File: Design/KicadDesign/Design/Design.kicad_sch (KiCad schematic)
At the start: 10 parts, among them J3 Jack 3.5 mm, Q1 IRLZ44N, Q2 IRLZ44N, U1 IR2110

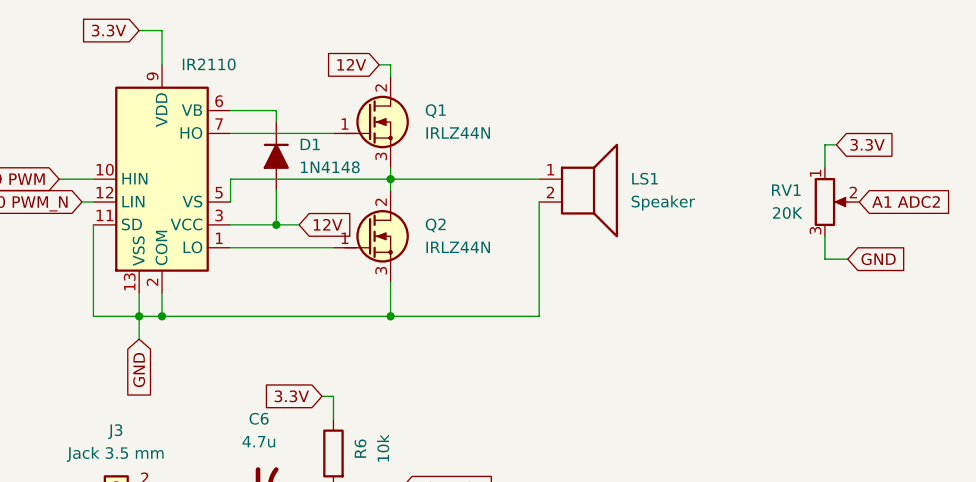
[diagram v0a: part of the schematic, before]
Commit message: Added Caps on VB TODO: Add STM32H523cet6 Footprint
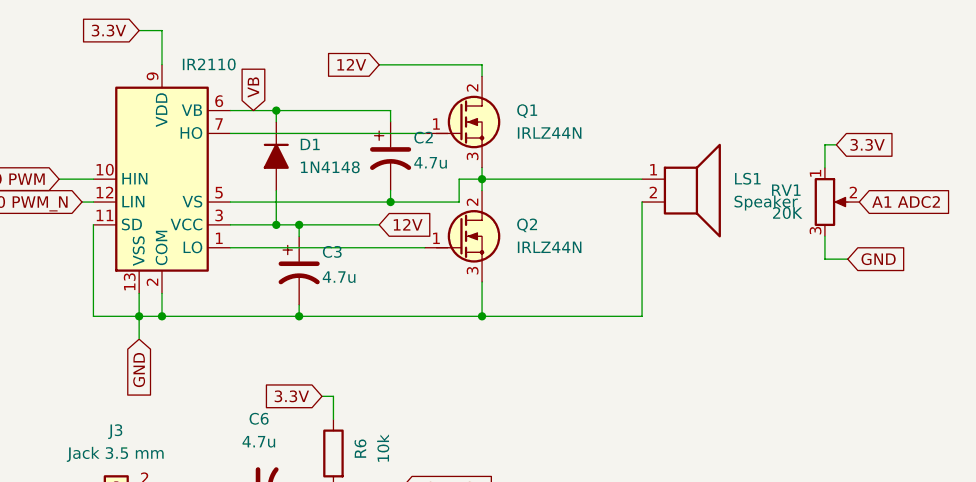
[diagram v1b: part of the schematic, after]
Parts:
- added C2, C3: 4.7u, Capacitor_THT:CP_Radial_D10.0mm_P3.50mm, symbol Device:C_Polarized_US
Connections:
- net 12V: now also C3.1
- net GND: now also C3.2
- net at LS1.1, Q1.3 (S), Q2.2 (D)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: now also C2.2
- net VB: now reaches D1.1 (K), U1.6 (VB)
- net VB: now also C2.1
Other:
- moved on the sheet: LS1, Q1, Q2

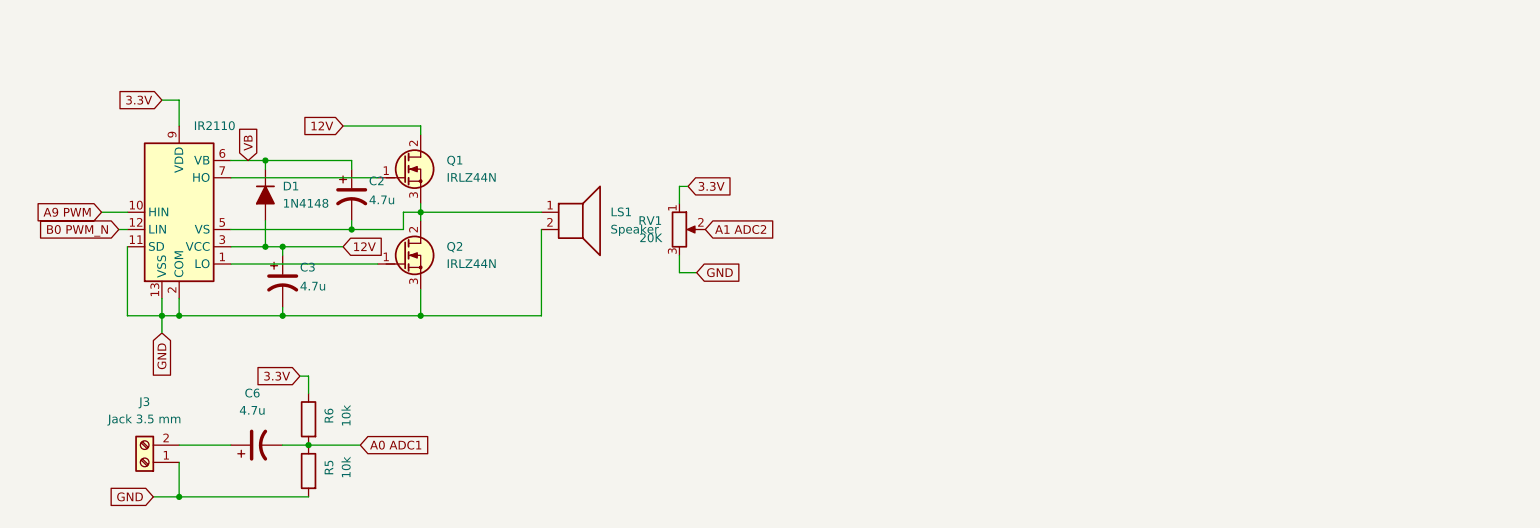
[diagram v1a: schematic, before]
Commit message: Added LC Filter
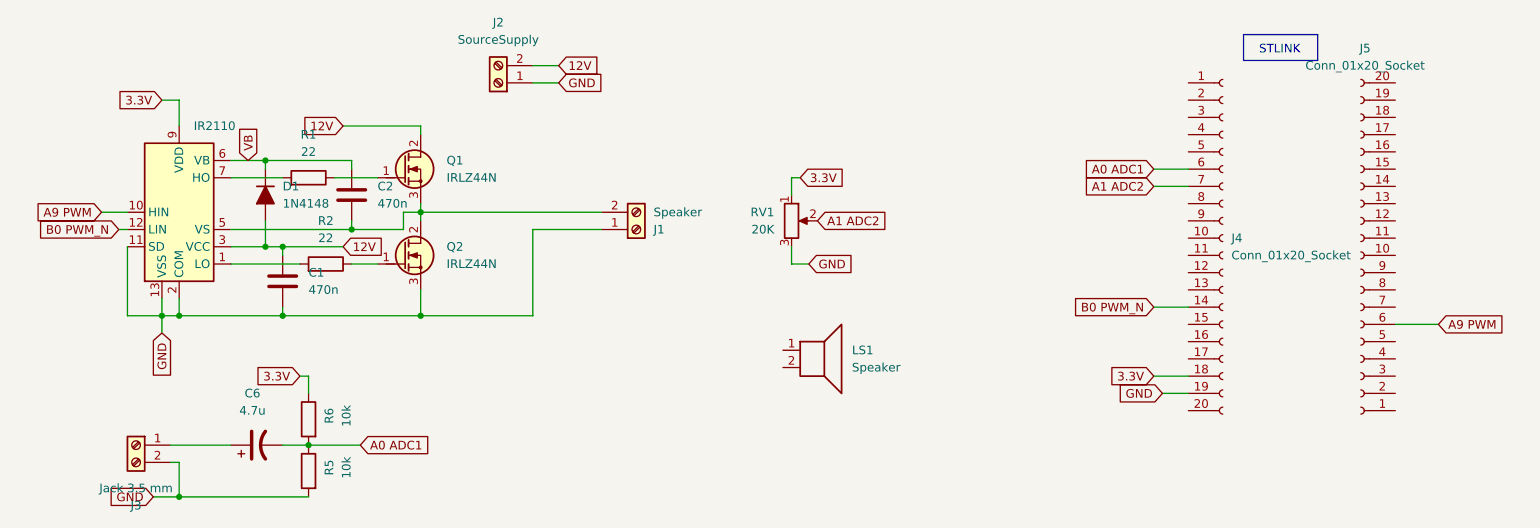
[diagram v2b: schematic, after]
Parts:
- removed C2, C3: 4.7u, Capacitor_THT:CP_Radial_D10.0mm_P3.50mm, symbol Device:C_Polarized_US
- added C1, C2: 470n, Capacitor_THT:C_Disc_D3.8mm_W2.6mm_P2.50mm, symbol PCM_Capacitor_AKL:C_0201
- added J1: Speaker, TerminalBlock:TerminalBlock_MaiXu_MX126-5.0-02P_1x02_P5.00mm, symbol Connector:Screw_Terminal_01x02
- added J2: SourceSupply, TerminalBlock:TerminalBlock_MaiXu_MX126-5.0-02P_1x02_P5.00mm, symbol Connector:Screw_Terminal_01x02
- added J4, J5: Conn_01x20_Socket, Connector_PinHeader_2.54mm:PinHeader_1x20_P2.54mm_Vertical, symbol Connector:Conn_01x20_Socket
- added R1, R2: 22, Resistor_THT:R_Axial_DIN0204_L3.6mm_D1.6mm_P7.62mm_Horizontal, symbol PCM_Resistor_AKL:R_0201
- C6: footprint Capacitor_THT:CP_Radial_D10.0mm_P3.50mm -> Capacitor_THT:CP_Radial_D5.0mm_P2.50mm
- LS1: footprint (none) -> Capacitor_THT:C_Disc_D4.3mm_W1.9mm_P5.00mm
- R5, R6: footprint Resistor_THT:R_Axial_DIN0207_L6.3mm_D2.5mm_P2.54mm_Vertical -> Resistor_THT:R_Axial_DIN0204_L3.6mm_D1.6mm_P7.62mm_Horizontal
- RV1: footprint (none) -> PCM_Potentiometer_THT_AKL:Potentiometer_Alps_RK163_Single_Horizontal
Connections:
- net 12V: now also C1.1, J2.2 (Pin_2)
- net 3.3V: now also J4.18 (Pin_18)
- net A0 ADC1: now also J4.6 (Pin_6)
- net A1 ADC2: now also J4.7 (Pin_7)
- net A9 PWM: now also J5.6 (Pin_6)
- net B0 PWM_N: now also J4.14 (Pin_14)
- net GND: now also J3.2 (Pin_2), C1.2, J1.1 (Pin_1), J2.1 (Pin_1), J4.19 (Pin_19); no longer J3.1 (Pin_1), LS1.2
- net VB: now also C2.1
- net at U1.1 (LO): now also R2.1; no longer Q2.1 (G)
- net at Q1.3 (S), Q2.2 (D), U1.5 (VS): now also C2.2, J1.2 (Pin_2); no longer LS1.1
- net at C6.1: now also J3.1 (Pin_1); no longer J3.2 (Pin_2)
- net at U1.7 (HO): now also R1.1; no longer Q1.1 (G)
- new net: Q2.1 (G), R2.2
- new net: Q1.1 (G), R1.2
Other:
- note added: "STLINK"
- moved on the sheet: J3, LS1, RV1

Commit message: Added NG-Pill
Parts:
- added C3: 470n, Capacitor_THT:C_Disc_D3.8mm_W2.6mm_P2.50mm, symbol PCM_Capacitor_AKL:C_0201
- added L1: L, Inductor_THT:L_Toroid_Horizontal_D7.8mm_P13.00mm_Diameter9-5mm_Amidon-T30, symbol Device:L
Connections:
- net GND: now also C3.2
- net at C2.2, Q1.3 (S), Q2.2 (D)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: now also L1.1; no longer J1.2 (Pin_2)
- new net: C3.1, J1.2 (Pin_2), L1.2
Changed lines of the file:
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@@
+	)
+	(junction
+		(at 116.84 43.18)
+		(diameter 0)
+		(color 0 0 0 0)
 	)
 	(junction
@@
 	)
 	(junction
+		(at 116.84 58.42)
+		(diameter 0)
+		(color 0 0 0 0)
+	)
+	(junction
 		(at 80.01 77.47)
 		(diameter 0)
@@
 	(wire
 		(pts
-			(xy 113.03 45.72) (xy 123.19 45.72)
-		)
-		(stroke
-			(width 0)
-			(type default)
-		)
-	)
-	(wire
-		(pts
 			(xy 52.07 45.72) (xy 53.34 45.72)
 		)
@@
 	(wire
 		(pts
-			(xy 113.03 58.42) (xy 96.52 58.42)
+			(xy 96.52 58.42) (xy 116.84 58.42)
 		)
 		(stroke
@@
 	(wire
 		(pts
-			(xy 113.03 45.72) (xy 113.03 58.42)
-		)
-		(stroke
-			(width 0)
-			(type default)
-		)
-	)
-	(wire
-		(pts
 			(xy 60.96 85.09) (xy 80.01 85.09)
 		)
@@
 	(wire
 		(pts
+			(xy 116.84 50.8) (xy 116.84 58.42)
+		)
+		(stroke
+			(width 0)
+			(type default)
+		)
+	)
+	(wire
+		(pts
 			(xy 73.66 44.45) (xy 73.66 48.26)
 		)
@@
 	(wire
 		(pts
+			(xy 116.84 58.42) (xy 123.19 58.42)
+		)
+		(stroke
+			(width 0)
+			(type default)
+		)
+	)
+	(wire
+		(pts
+			(xy 96.52 43.18) (xy 106.68 43.18)
+		)
+		(stroke
+			(width 0)
+			(type default)
+		)
+	)
+	(wire
+		(pts
 			(xy 86.36 36.83) (xy 86.36 35.56)
 		)
@@
 	(wire
 		(pts
+			(xy 123.19 58.42) (xy 123.19 45.72)
+		)
+		(stroke
+			(width 0)
+			(type default)
+		)
+	)
+	(wire
+		(pts
 			(xy 80.01 77.47) (xy 87.63 77.47)
 		)
@@
 	(wire
 		(pts
-			(xy 96.52 43.18) (xy 123.19 43.18)
-		)
-		(stroke
-			(width 0)
-			(type default)
-		)
-	)
-	(wire
-		(pts
 			(xy 60.96 58.42) (xy 76.2 58.42)
 		)
@@
 	(wire
 		(pts
+			(xy 114.3 43.18) (xy 116.84 43.18)
+		)
+		(stroke
+			(width 0)
+			(type default)
+		)
+	)
+	(wire
+		(pts
 			(xy 93.98 45.72) (xy 93.98 43.18)
 		)
@@
 		(pts
 			(xy 96.52 43.18) (xy 96.52 44.45)
+		)
+		(stroke
+			(width 0)
+			(type default)
+		)
+	)
+	(wire
+		(pts
+			(xy 116.84 43.18) (xy 123.19 43.18)
 		)
 		(stroke
@@
 	)
 	(symbol
+		(lib_id "PCM_Capacitor_AKL:C_0201")
+		(at 116.84 46.99 0)
+		(unit 1)
+		(exclude_from_sim no)
+		(in_bom yes)
+		(on_board yes)
+		(dnp no)
+		(fields_autoplaced yes)
+		(property "Reference" "C3"
+			(at 120.65 45.7199 0)
+			(effects
+				(font
+					(size 1.27 1.27)
+				)
+				(justify left)
+			)
+		)
+		(property "Value" "470n"
+			(at 120.65 48.2599 0)
+			(effects
+				(font
+					(size 1.27 1.27)
+				)
+				(justify left)
+			)
+		)
+		(property "Footprint" "Capacitor_THT:C_Disc_D3.8mm_W2.6mm_P2.50mm"
+			(at 117.8052 50.8 0)
+			(effects
+				(font
+					(size 1.27 1.27)
+				)
+				(hide yes)
+			)
+		)
+		(property "Datasheet" "~"
+			(at 116.84 46.99 0)
+			(effects
+				(font
+					(size 1.27 1.27)
+				)
+				(hide yes)
+			)
+		)
+		(property "Description" "SMD 0201 MLCC capacitor, Alternate KiCad Library"
+			(at 116.84 46.99 0)
+			(effects
+				(font
+					(size 1.27 1.27)
+				)
+				(hide yes)
+			)
+		)
+		(pin "1"
+		)
+		(pin "2"
+		)
+		(instances
+			(project "Design"
+				(path "/40006f24-a25a-439b-add0-ed3afa522b6a"
+					(reference "C3")
+					(unit 1)
+				)
+			)
+		)
+	)
+	(symbol
 		(lib_id "Connector:Conn_01x20_Socket")
 		(at 234.95 49.53 180)
@@
 					(unit 1)
 				)
+			)
+		)
+	)
+	(symbol
+		(lib_id "Device:L")
+		(at 110.49 43.18 90)
+		(unit 1)
+		(exclude_from_sim no)
+		(in_bom yes)
+		(on_board yes)
+		(dnp no)
+		(fields_autoplaced yes)
+		(property "Reference" "L1"
+			(at 110.49 38.1 90)
+			(effects
+				(font
+					(size 1.27 1.27)
+				)
+			)
+		)
+		(property "Value" "L"
+			(at 110.49 40.64 90)
+			(effects
+				(font
+					(size 1.27 1.27)
+				)
+			)
+		)
+		(property "Footprint" "Inductor_THT:L_Toroid_Horizontal_D7.8mm_P13.00mm_Diameter9-5mm_Amidon-T30"
+			(at 110.49 43.18 0)
+			(effects
+				(font
+					(size 1.27 1.27)
+				)
+				(hide yes)
+			)
+		)
+		(property "Datasheet" "~"
+			(at 110.49 43.18 0)
+			(effects
+				(font
+					(size 1.27 1.27)
+				)
+				(hide yes)
+			)
+		)
+		(property "Description" "Inductor"
+			(at 110.49 43.18 0)
+			(effects
+				(font
+					(size 1.27 1.27)
+				)
+				(hide yes)
+			)
+		)
+		(pin "2"
+		)
+		(pin "1"
+		)
+		(instances
+			(project ""
+				(path "/40006f24-a25a-439b-add0-ed3afa522b6a"
+					(reference "L1")
+					(unit 1)
+				)

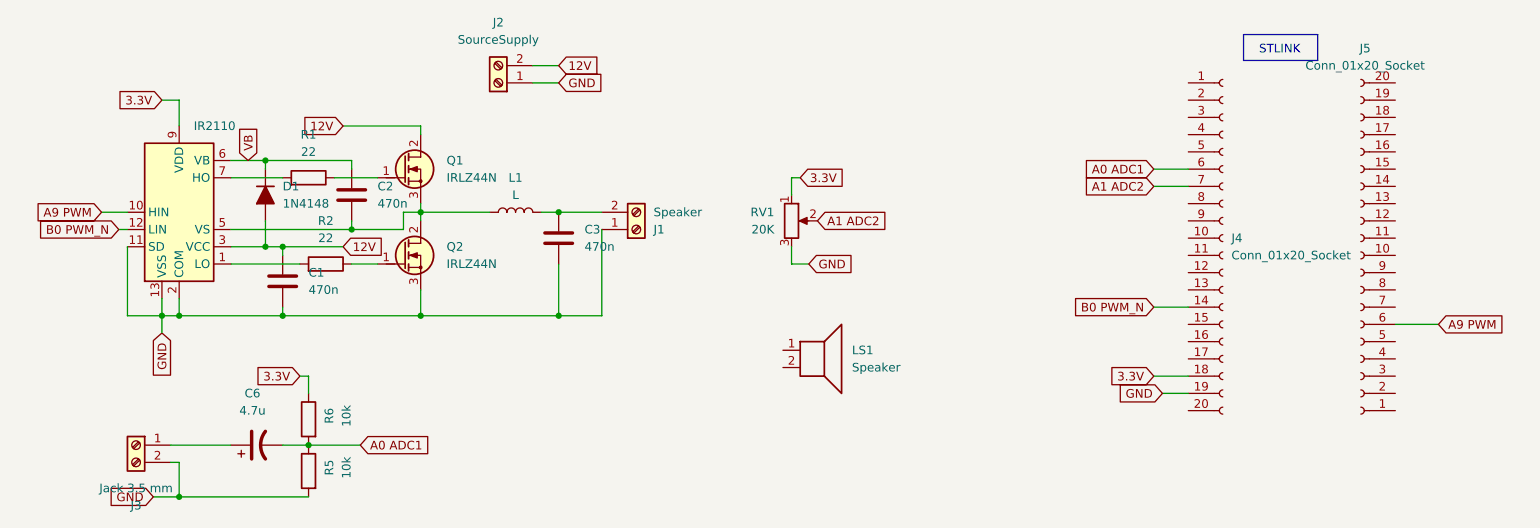
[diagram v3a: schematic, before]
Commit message: Updated pin B0->B1 A9->A10
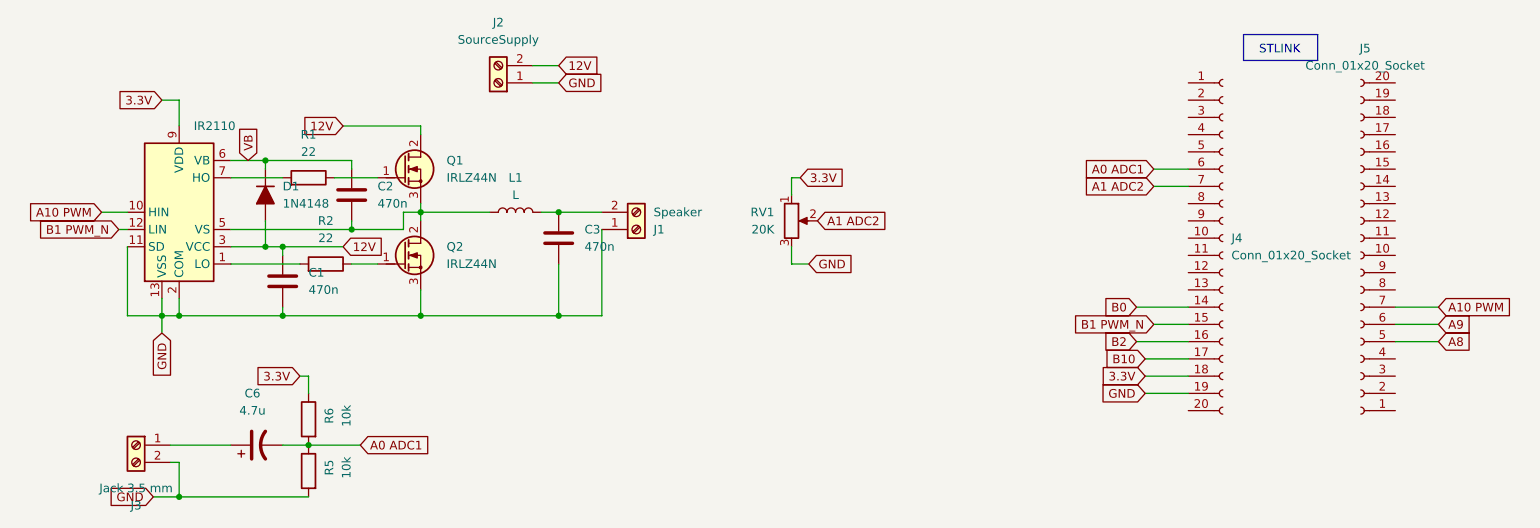
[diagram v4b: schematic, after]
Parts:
- removed LS1: Speaker, Capacitor_THT:C_Disc_D4.3mm_W1.9mm_P5.00mm, symbol Device:Speaker
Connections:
- net A8: now reaches J5.5 (Pin_5)
- net A10 PWM: now reaches J5.7 (Pin_7)
- net A10 PWM: now also U1.10 (HIN)
- net B1 PWM_N: now reaches J4.15 (Pin_15)
- net B1 PWM_N: now also U1.12 (LIN)
- net B2: now reaches J4.16 (Pin_16)
- net B10: now reaches J4.17 (Pin_17)
- net A9 PWM renamed A9
- net A9: no longer U1.10 (HIN)
- net B0 PWM_N renamed B0
- net B0: no longer U1.12 (LIN)
